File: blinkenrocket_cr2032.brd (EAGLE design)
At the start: 96.3 x 47 mm, 22 parts, among them SW1 SWITCH-4POMRON-6-6-SWITCH, SW2 SWITCH-4POMRON-6-6-SWITCH, U2 EEPROM-I2CEIAJ

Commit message: change value of modem input resistor
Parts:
- R3: value 33 -> 16
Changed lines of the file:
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@@
 <attribute name="VALUE" x="43.7515" y="34.2265" size="1.016" layer="28" ratio="10" rot="MR90"/>
 </element>
-<element name="R3" library="resistor" package="R1206" value="33" x="23.495" y="35.56" smashed="yes" rot="MR270">
+<element name="R3" library="resistor" package="R1206" value="16" x="23.495" y="35.56" smashed="yes" rot="MR270">
 <attribute name="NAME" x="22.606" y="38.6715" size="1.016" layer="26" ratio="10" rot="MR90"/>
 <attribute name="VALUE" x="24.7015" y="34.8615" size="1.016" layer="28" ratio="10" rot="MR90"/>

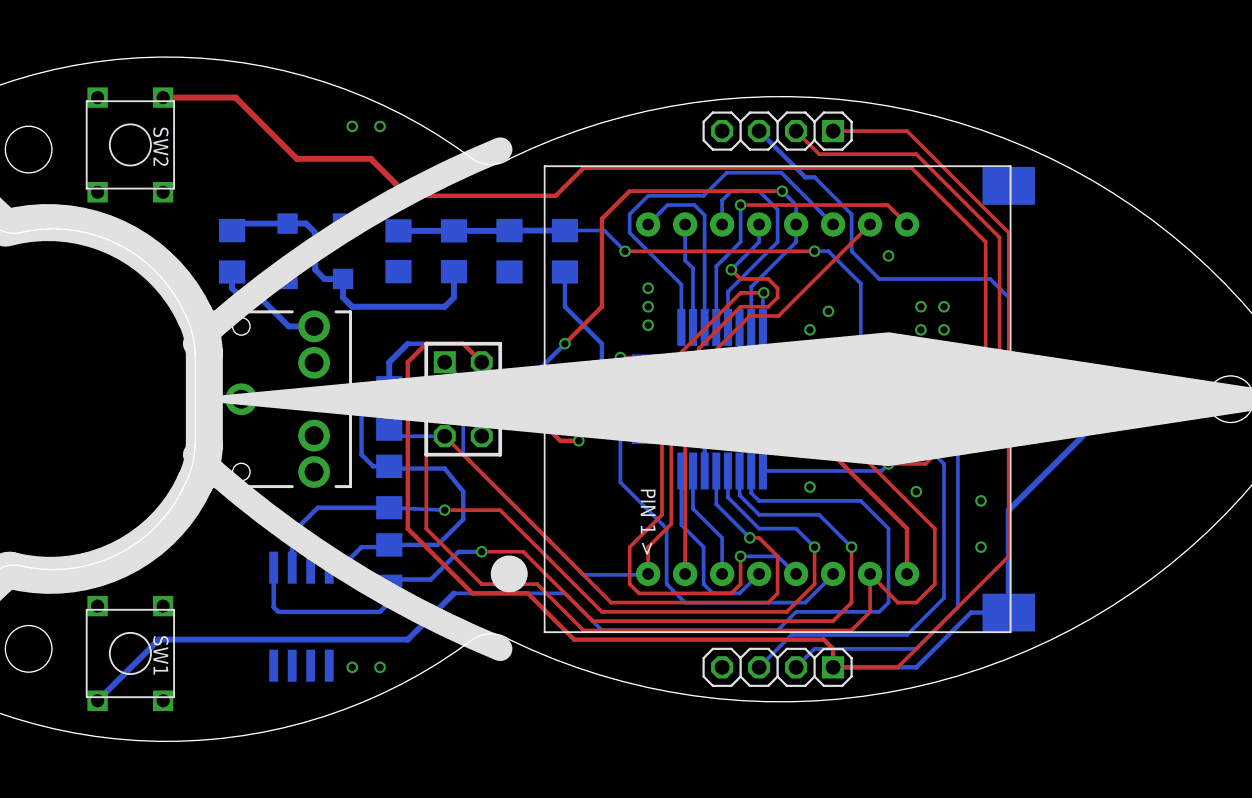
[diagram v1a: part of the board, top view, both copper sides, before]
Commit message: Revision 2c - diodes do have positioning information now - added blinkenrocket.de text - add IC component name
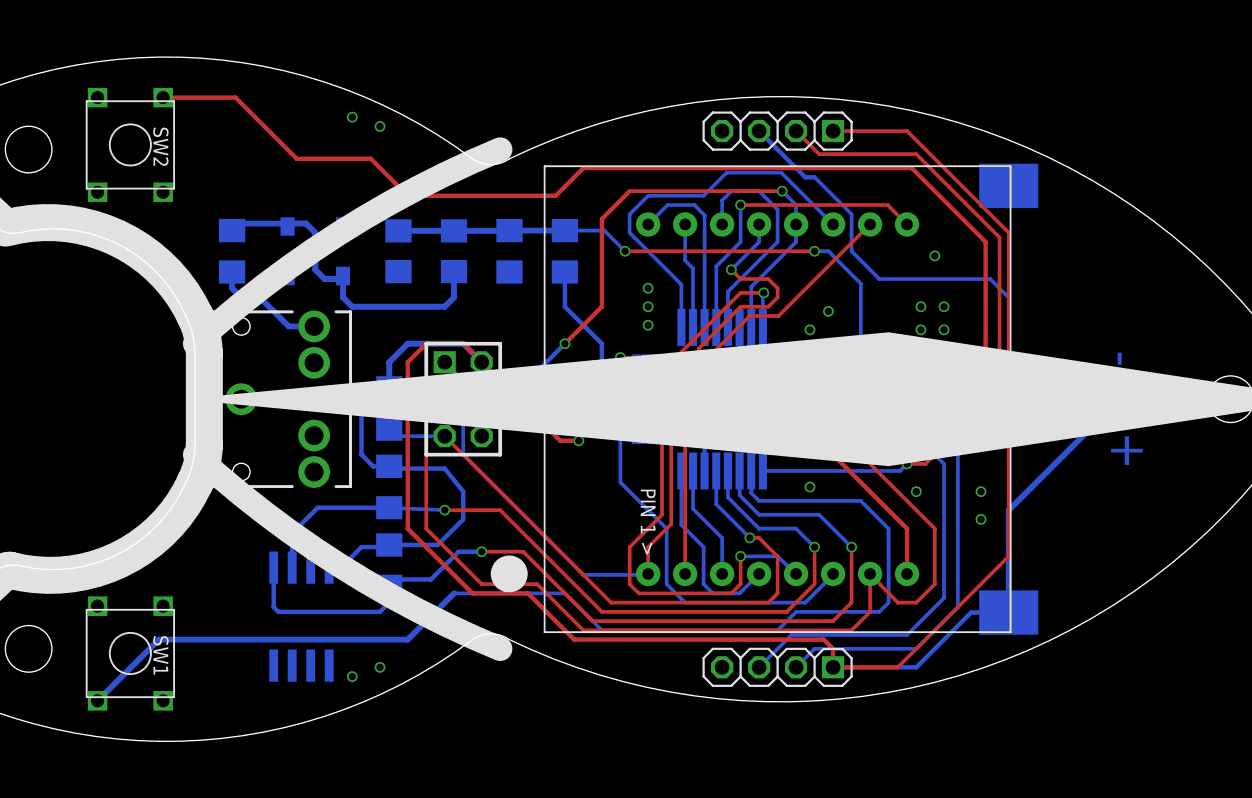
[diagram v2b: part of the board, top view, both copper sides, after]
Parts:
- D1, D2: device diode-1:SOD123 -> ipc-7351-diode:SOD3718X135N
- U$2: value ATTINY88 -> U1
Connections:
- net GND: now also D1.K; no longer D1.C
- net N$3: now also D2.K; no longer D2.C
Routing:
- net N$3: track 22.1 -> 22.9 mm
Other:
- board text added: "Rev 2c"
- board text added: "blinkenrocket.de"
- board text removed: "Rev 2b"
